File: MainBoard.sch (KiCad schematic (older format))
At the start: 89 parts, among them J1 DB25, P1 BOOT, P10 CONN_01X03, P11 CONN_01X03, P12 CONN_01X03, P13 CONN_01X03, P14 CONN_01X02, P15 CONN_02X07, P16 CONN_02X04, P18 CONN_01X03, P2 CONN_01X04, P3 CONN_02X04, P4 HOLE, P5 HOLE, P6 HOLE, P7 HOLE, P8 CONN_01X02, P9 CONN_01X03, Q1 BSS138, Q2 BSS138, Q3 DMN65D8L, SW1 RESET, U1 mp2307, U10 SI4425DDY, U11 INA199A2, U12 ADS1015, U2 DYS_mini_ESC, U3 DYS_mini_ESC, U4 DYS_mini_ESC, U5 DYS_mini_ESC, U6 TLV1117LV33, U7 TENDA_P200, U8 pca9685, U9 STM32F103CBT6, Y1 8MHz

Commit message: Update BOM
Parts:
- C10, C11: deviceMart (none) -> 8195
- C12: deviceMart (none) -> 34759
- C13, C14: deviceMart (none) -> 19164
- C15, C16, C17, C18, C22: deviceMart (none) -> 35827
- C19: deviceMart (none) -> 4253
- C2, C20, C23, C24: deviceMart (none) -> 8088
- C3: deviceMart (none) -> 19159
- C4: deviceMart (none) -> 34758
- C6, C7, C8, C9: DeviceMart (none) -> 6791
- R1: deviceMart (none) -> 6134
- R10, R11, R13, R14, R15, R16, R5, R8, R9: deviceMart (none) -> 107779
- R17: deviceMart (none) -> 1077781
- R18, R19, R6, R7: deviceMart (none) -> 19220
- R20: deviceMart (none) -> 19211
- R21: value 30.1k %1 -> 30.1k 1%; digiKey (none) -> 311-2529-1-ND
- R3: value 10k 1% -> 10k %1
- U9: deviceMart (none) -> 1163085
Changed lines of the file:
@@
 F 2 "Capacitors_SMD:CP_Elec_8x10" H 4475 1000 50  0001 C CNN
 F 3 "" H 4475 1000 50  0000 C CNN
+F 4 "6791" H 4475 1000 60  0001 C CNN "DeviceMart"
 	1    4475 1000
 	-1   0    0    1
@@
 F 2 "Capacitors_SMD:CP_Elec_8x10" H 4475 1775 50  0001 C CNN
 F 3 "" H 4475 1775 50  0000 C CNN
+F 4 "6791" H 4475 1775 60  0001 C CNN "DeviceMart"
 	1    4475 1775
 	-1   0    0    1
@@
 F 2 "Capacitors_SMD:CP_Elec_8x10" H 4475 2550 50  0001 C CNN
 F 3 "" H 4475 2550 50  0000 C CNN
+F 4 "6791" H 4475 2550 60  0001 C CNN "DeviceMart"
 	1    4475 2550
 	-1   0    0    1
@@
 F 2 "Capacitors_SMD:CP_Elec_8x10" H 4475 3350 50  0001 C CNN
 F 3 "" H 4475 3350 50  0000 C CNN
+F 4 "6791" H 4475 3350 60  0001 C CNN "DeviceMart"
 	1    4475 3350
 	-1   0    0    1
@@
 F 2 "footprint:r_0603" V 1405 1050 50  0001 C CNN
 F 3 "" H 1475 1050 50  0000 C CNN
+F 4 "6134" H 1475 1050 60  0001 C CNN "deviceMart"
 	1    1475 1050
 	1    0    0    -1
@@
 F 2 "footprint:c_0603" H 1513 1600 50  0001 C CNN
 F 3 "" H 1475 1750 50  0000 C CNN
+F 4 "8088" H 1475 1750 60  0001 C CNN "deviceMart"
 	1    1475 1750
 	1    0    0    -1
@@
 F 2 "footprint:c_0603" H 2365 1984 50  0001 L CNN
 F 3 "" H 2250 2075 50  0000 C CNN
+F 4 "19159" H 2250 2075 60  0001 C CNN "deviceMart"
 	1    2250 2075
 	1    0    0    -1
@@
 F 2 "footprint:c_0603" V 2415 825 50  0001 C CNN
 F 3 "" H 2575 825 50  0000 C CNN
+F 4 "34758" V 2575 825 60  0001 C CNN "deviceMart"
 	1    2575 825
 	0    1    1    0
@@
 P 2925 2075
 F 0 "R3" H 2995 2121 50  0000 L CNN
-F 1 "10k 1%" V 2825 1950 50  0000 L CNN
+F 1 "10k %1" V 2825 1950 50  0000 L CNN
 F 2 "footprint:r_0603" V 2855 2075 50  0001 C CNN
 F 3 "" H 2925 2075 50  0000 C CNN
@@
 F 2 "footprint:c_0805" H 1390 3384 50  0001 L CNN
 F 3 "" H 1275 3475 50  0000 C CNN
+F 4 "8195" H 1275 3475 60  0001 C CNN "deviceMart"
 	1    1275 3475
 	1    0    0    -1
@@
 F 2 "footprint:c_0805" H 2990 3384 50  0001 L CNN
 F 3 "" H 2875 3475 50  0000 C CNN
+F 4 "8195" H 2875 3475 60  0001 C CNN "deviceMart"
 	1    2875 3475
 	1    0    0    -1
@@
 F 2 "footprint:r_0603" V 1355 5250 50  0001 C CNN
 F 3 "" H 1425 5250 50  0000 C CNN
+F 4 "19220" V 1425 5250 60  0001 C CNN "deviceMart"
 	1    1425 5250
 	0    1    1    0
@@
 F 2 "footprint:r_0603" V 1355 5450 50  0001 C CNN
 F 3 "" H 1425 5450 50  0000 C CNN
+F 4 "19220" V 1425 5450 60  0001 C CNN "deviceMart"
 	1    1425 5450
 	0    1    1    0
@@
 F 2 "footprint:c_0603" H 7590 984 50  0001 L CNN
 F 3 "" H 7475 1075 50  0000 C CNN
+F 4 "34759" H 7475 1075 60  0001 C CNN "deviceMart"
 	1    7475 1075
 	1    0    0    -1
@@
 F 2 "footprint:r_0603" V 7655 1375 50  0001 C CNN
 F 3 "" H 7725 1375 50  0000 C CNN
+F 4 "107779" V 7725 1375 60  0001 C CNN "deviceMart"
 	1    7725 1375
 	0    1    1    0
@@
 F 2 "footprint:r_0603" V 1055 6500 50  0001 C CNN
 F 3 "" H 1125 6500 50  0000 C CNN
+F 4 "107779" H 1125 6500 60  0001 C CNN "deviceMart"
 	1    1125 6500
 	1    0    0    -1
@@
 F 2 "footprint:r_0603" V 1730 6500 50  0001 C CNN
 F 3 "" H 1800 6500 50  0000 C CNN
+F 4 "107779" H 1800 6500 60  0001 C CNN "deviceMart"
 	1    1800 6500
 	1    0    0    -1
@@
 F 2 "footprint:r_0603" V 2830 6500 50  0001 C CNN
 F 3 "" H 2900 6500 50  0000 C CNN
+F 4 "107779" H 2900 6500 60  0001 C CNN "deviceMart"
 	1    2900 6500
 	1    0    0    -1
@@
 F 2 "footprint:r_0603" V 3505 6500 50  0001 C CNN
 F 3 "" H 3575 6500 50  0000 C CNN
+F 4 "107779" H 3575 6500 60  0001 C CNN "deviceMart"
 	1    3575 6500
 	1    0    0    -1
@@
 F 3 "" H 11850 7800 50  0000 C CNN
 F 4 "497-6288-ND" H 11850 7800 60  0001 C CNN "DigiKey"
+F 5 "1163085" H 11850 7800 60  0001 C CNN "deviceMart"
 	1    11850 7800
 	1    0    0    -1
@@
 F 2 "footprint:c_0603" H 11263 5625 50  0001 C CNN
 F 3 "" H 11225 5775 50  0000 C CNN
+F 4 "35827" H 11225 5775 60  0001 C CNN "deviceMart"
 	1    11225 5775
 	1    0    0    -1
@@
 F 2 "footprint:c_0603" H 11463 5625 50  0001 C CNN
 F 3 "" H 11425 5775 50  0000 C CNN
+F 4 "35827" H 11425 5775 60  0001 C CNN "deviceMart"
 	1    11425 5775
 	1    0    0    -1
@@
 F 2 "footprint:c_0603" H 10863 5625 50  0001 C CNN
 F 3 "" H 10825 5775 50  0000 C CNN
+F 4 "35827" H 10825 5775 60  0001 C CNN "deviceMart"
 	1    10825 5775
 	1    0    0    -1
@@
 F 2 "footprint:c_0603" H 11063 5625 50  0001 C CNN
 F 3 "" H 11025 5775 50  0000 C CNN
+F 4 "35827" H 11025 5775 60  0001 C CNN "deviceMart"
 	1    11025 5775
 	1    0    0    -1
@@
 F 2 "footprint:r_0603" H 8870 6084 50  0001 L CNN
 F 3 "" H 8800 6175 50  0000 C CNN
+F 4 "107779" V 8800 6175 60  0001 C CNN "deviceMart"
 	1    8800 6175
 	1    0    0    -1
@@
 F 2 "footprint:r_0603" H 8745 6084 50  0001 L CNN
 F 3 "" H 8675 6175 50  0000 C CNN
+F 4 "107779" V 8675 6175 60  0001 C CNN "deviceMart"
 	1    8675 6175
 	1    0    0    -1
@@
 F 2 "footprint:c_0603" V 7240 7200 50  0001 C CNN
 F 3 "" H 7400 7200 50  0000 C CNN
+F 4 "19164" V 7400 7200 60  0001 C CNN "deviceMart"
 	1    7400 7200
 	0    1    1    0
@@
 F 2 "footprint:c_0603" V 7240 7500 50  0001 C CNN
 F 3 "" H 7400 7500 50  0000 C CNN
+F 4 "19164" V 7400 7500 60  0001 C CNN "deviceMart"
 	1    7400 7500
 	0    1    1    0
@@
 F 2 "footprint:r_0603" H 4745 4159 50  0001 L CNN
 F 3 "" H 4675 4250 50  0000 C CNN
+F 4 "107779" V 4675 4250 60  0001 C CNN "deviceMart"
 	1    4675 4250
 	1    0    0    -1
@@
 F 2 "footprint:r_0603" H 4745 4459 50  0001 L CNN
 F 3 "" H 4675 4550 50  0000 C CNN
+F 4 "1077781" V 4675 4550 60  0001 C CNN "deviceMart"
 	1    4675 4550
 	1    0    0    -1
@@
 F 2 "footprint:r_0603" H 4270 4959 50  0001 L CNN
 F 3 "" H 4200 5050 50  0000 C CNN
+F 4 "107779" V 4200 5050 60  0001 C CNN "deviceMart"
 	1    4200 5050
 	1    0    0    -1
@@
 F 2 "footprint:r_0603" V 15030 9325 50  0001 C CNN
 F 3 "" H 15100 9325 50  0000 C CNN
+F 4 "19220" V 15100 9325 60  0001 C CNN "deviceMart"
 	1    15100 9325
 	-1   0    0    1
@@
 F 2 "footprint:r_0603" V 15230 9325 50  0001 C CNN
 F 3 "" H 15300 9325 50  0000 C CNN
+F 4 "19220" V 15300 9325 60  0001 C CNN "deviceMart"
 	1    15300 9325
 	-1   0    0    1
@@
 F 2 "Capacitors_SMD:CP_Elec_6.3x5.8" H 925 3475 50  0001 C CNN
 F 3 "" H 925 3475 50  0000 C CNN
+F 4 "4253" H 925 3475 60  0001 C CNN "deviceMart"
 	1    925  3475
 	1    0    0    -1
@@
 F 2 "footprint:c_0603" H 9240 4334 50  0001 L CNN
 F 3 "" H 9125 4425 50  0000 C CNN
+F 4 "8088" H 9125 4425 60  0001 C CNN "deviceMart"
 	1    9125 4425
 	1    0    0    -1
@@
 F 2 "footprint:r_0603" V 9605 4425 50  0001 C CNN
 F 3 "" H 9675 4425 50  0000 C CNN
+F 4 "19211" V 9675 4425 60  0001 C CNN "deviceMart"
 	1    9675 4425
 	0    1    1    0
@@
 F 2 "footprint:c_0603" H 9900 4625 50  0001 C CNN
 F 3 "" H 9900 4625 50  0000 C CNN
+F 4 "35827" H 9900 4625 60  0001 C CNN "deviceMart"
 	1    9900 4625
 	1    0    0    -1
@@
 P 10925 4075
 F 0 "R21" H 11000 4075 50  0000 L CNN
-F 1 "30.1k %1" V 10825 3900 50  0000 L CNN
+F 1 "30.1k 1%" V 10825 3900 50  0000 L CNN
 F 2 "footprint:r_0603" V 10855 4075 50  0001 C CNN
 F 3 "" H 10925 4075 50  0000 C CNN
+F 4 "311-2529-1-ND" H 10925 4075 60  0001 C CNN "digiKey"
 	1    10925 4075
 	1    0    0    -1
@@
 F 2 "footprint:c_0603" H 11338 4350 50  0001 C CNN
 F 3 "" H 11300 4500 50  0000 C CNN
+F 4 "8088" H 11300 4500 60  0001 C CNN "deviceMart"
 	1    11300 4500
 	1    0    0    -1
@@
 F 2 "footprint:c_0603" H 14563 4250 50  0001 C CNN
 F 3 "" H 14525 4400 50  0000 C CNN
+F 4 "8088" H 14525 4400 60  0001 C CNN "deviceMart"
 	1    14525 4400
 	1    0    0    -1

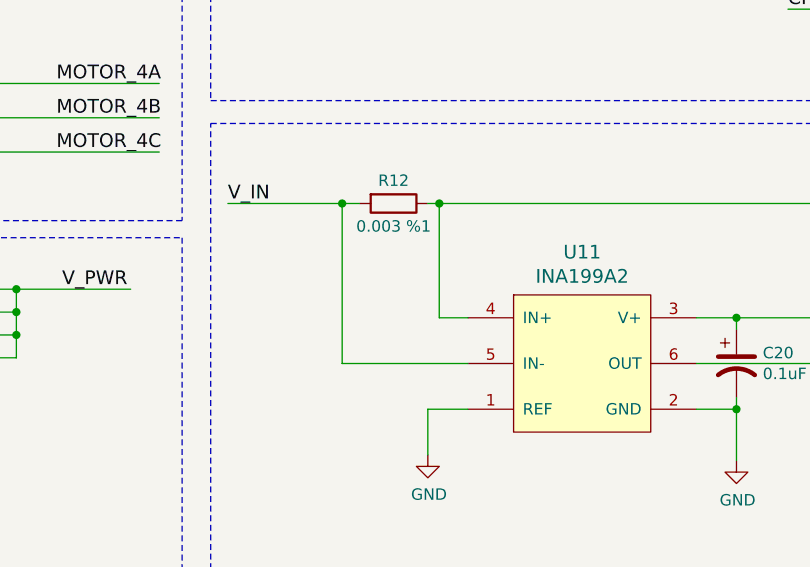
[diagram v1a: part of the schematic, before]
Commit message: Fix ina199a2 routing
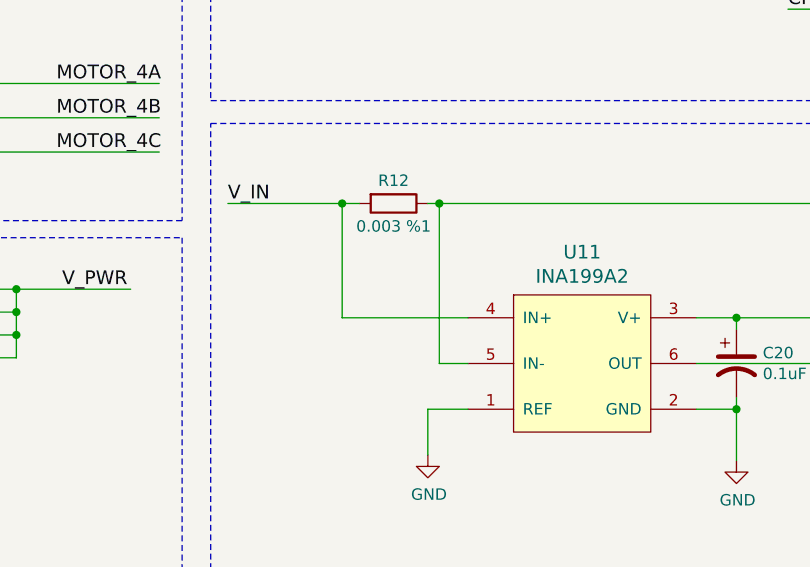
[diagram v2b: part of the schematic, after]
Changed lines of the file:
@@
 	1    0    0    -1
 $EndComp
-Wire Wire Line
-	7825 3725 7825 4225
-Wire Wire Line
-	7825 4225 7950 4225
 Connection ~ 7825 3725
-Wire Wire Line
-	7400 3725 7400 4425
-Wire Wire Line
-	7400 4425 7950 4425
 Connection ~ 7400 3725
 Text Label 11675 3725 0    60   ~ 0
@@
 Text Notes 13900 5250 0    60   Italic 0
 Current & Voltage sensing
+Wire Wire Line
+	7950 4225 7400 4225
+Wire Wire Line
+	7400 4225 7400 3725
+Wire Wire Line
+	7825 3725 7825 4425
+Wire Wire Line
+	7825 4425 7950 4425
 $EndSCHEMATC
